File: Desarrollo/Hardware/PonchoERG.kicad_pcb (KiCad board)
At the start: 2 copper layers, 85.9 x 80.5 mm, 112 parts, among them J1 Entradas Analógicas, J2 IOs Multipropósito, U1 TPD2E001, U10 ADS1299, U11 ADuM6401, U12 ADuM2401, U13 NCP1117ST33T3G, U14 OPA2376, U15 TPD2E001, U2 TPD2E001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

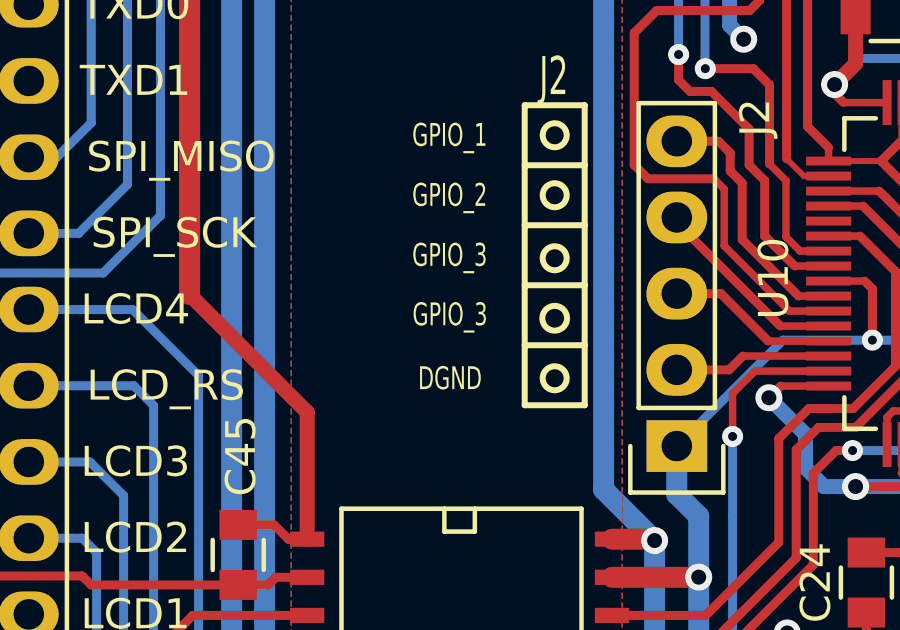
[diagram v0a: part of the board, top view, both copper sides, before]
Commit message: Corrección de etiqueta de serigrafía en J2. Se cambió GPIO_3 que estaba repetido por GPIO_4.
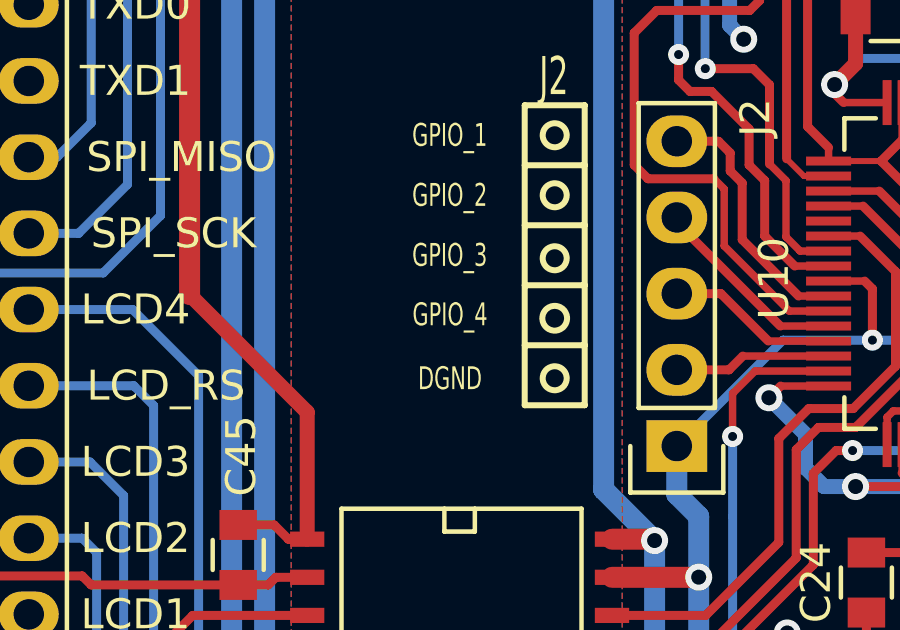
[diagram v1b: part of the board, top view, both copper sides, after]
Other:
- board text added: "GPIO_4"
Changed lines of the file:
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@@
     (links 263)
     (no_connects 0)
-    (area 99.934999 67.844999 185.955001 148.495001)
+    (area 17.422141 17.62 209.466108 164.140001)
     (thickness 1.6)
     (drawings 64)
@@
     (effects (font (size 0.762 0.508) (thickness 0.127)))
   )
-  (gr_text GPIO_3 (at 123.26 108.89) (layer F.SilkS)
+  (gr_text GPIO_4 (at 123.26 108.89) (layer F.SilkS)
     (effects (font (size 0.762 0.508) (thickness 0.127)))
   )

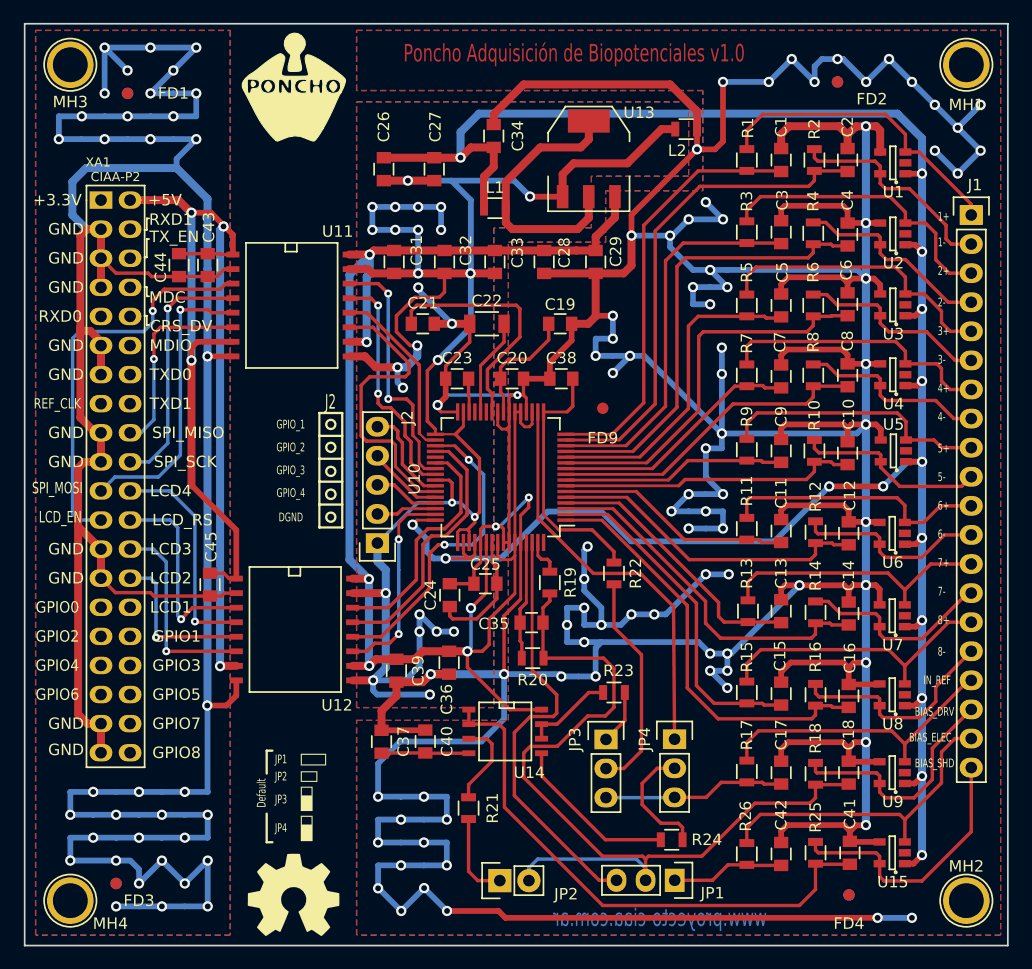
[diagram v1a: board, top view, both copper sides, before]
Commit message: Actualización de PCB. Cotas de diseño. Generación de BOM. Archivos Gerber disponibles en carpeta "gerbers". Colocación de eje auxiliar de posicionamiento en mounting hole inferior izquierdo. Actualización de esquemático con modificación de comentarios y adición de código de compra DigiKey y hoja de datos en algunos componentes que faltaban. FINALIZADO
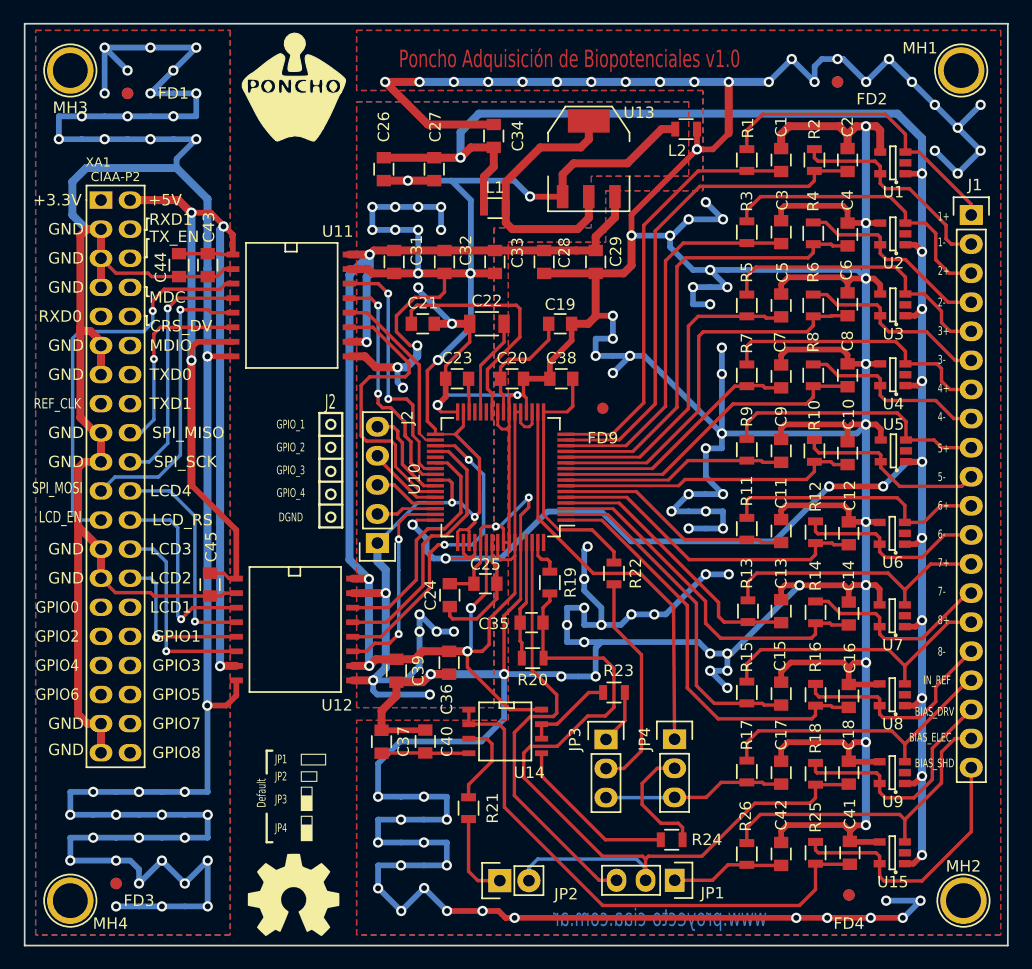
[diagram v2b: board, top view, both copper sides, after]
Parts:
- removed Slot_1: Fiducial, Fiducials:Fiducial_1mm_Dia_2.54mm_Outer_CopperTop
- removed Slot_2: Slot_2, Fiducials:Fiducial_1mm_Dia_2.54mm_Outer_CopperTop
- added SC_1: Slot_1, Fiducials:Fiducial_1mm_Dia_2.54mm_Outer_CopperTop, F.Cu at (123.3, 92.5)
- added SC_2: Slot_2, Fiducials:Fiducial_1mm_Dia_2.54mm_Outer_CopperTop, F.Cu at (123.6, 120.8)
- moved MH1 0.67 mm to (181.8, 72.0)
- moved MH3 0.50 mm to (104.0, 72.0)
- moved MH2 0.25 mm to (182.0, 144.5)
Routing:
- net GNDA: track 656.0 -> 678.8 mm, vias 89 -> 105
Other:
- board text removed: "Zona_Corte"
